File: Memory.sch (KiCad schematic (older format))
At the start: 8 parts, among them U2 24FC128, U3 W25Q128FW

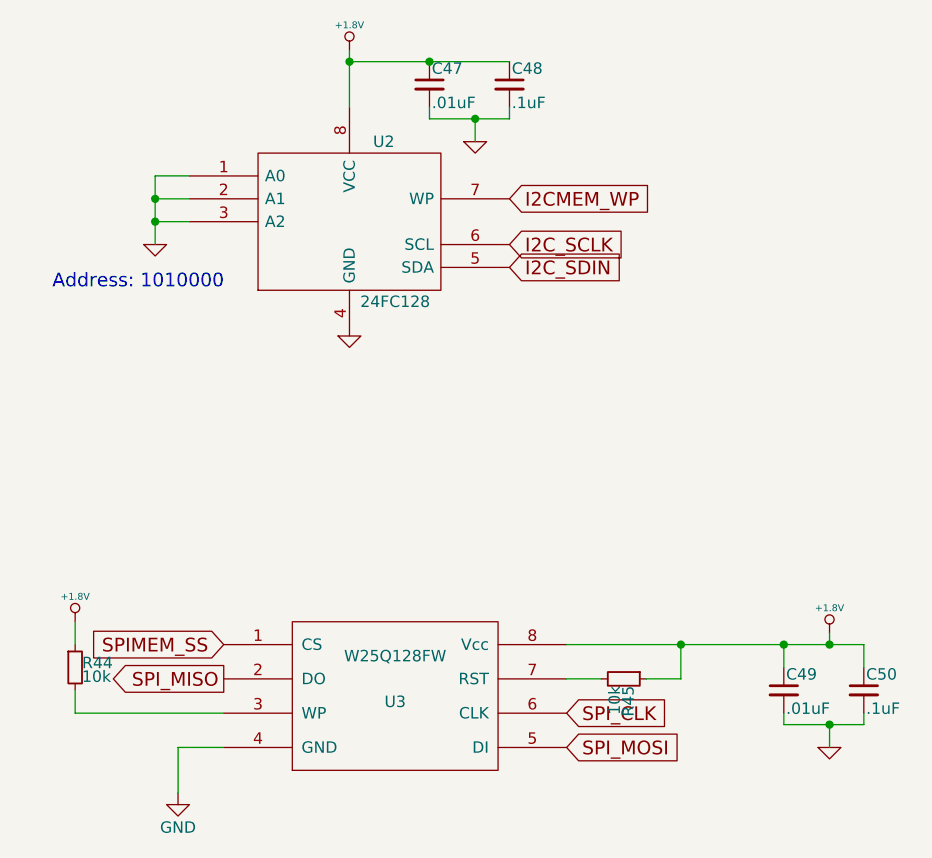
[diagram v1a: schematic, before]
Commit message: finished wiring GPIF with exception of PCLK
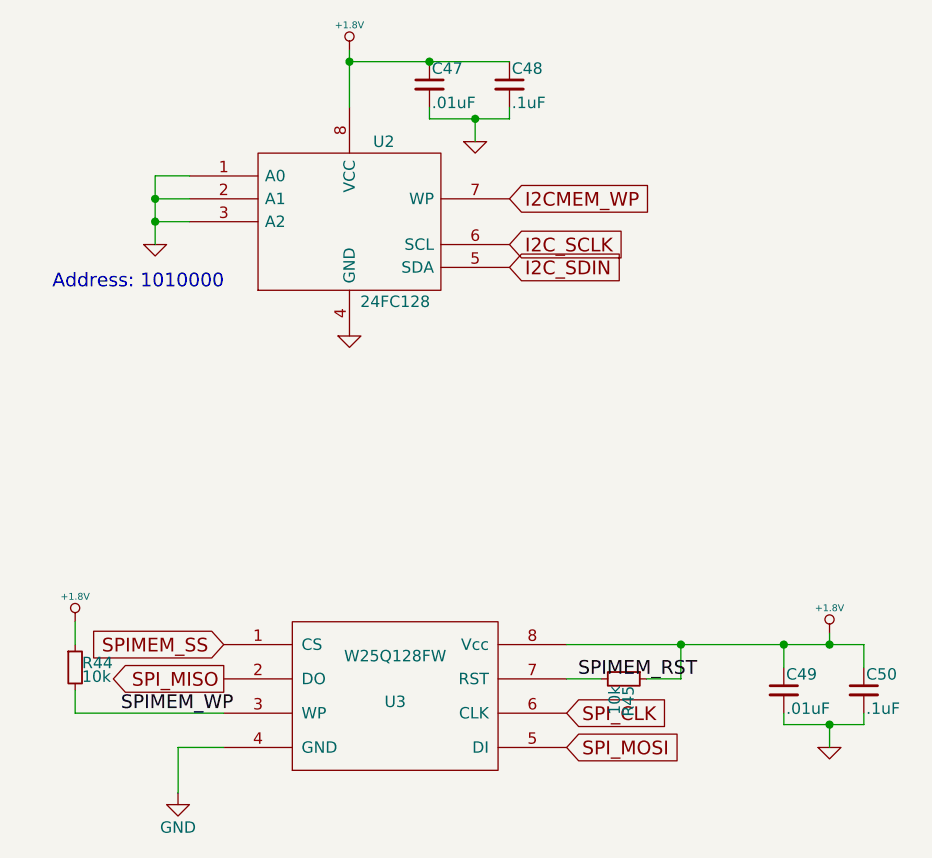
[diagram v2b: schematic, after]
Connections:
- net SPIMEM_WP: now reaches R44.2, U3.3 (WP)
- net SPIMEM_RST: now reaches R45.2, U3.7 (RST)
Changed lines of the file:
@@
 	6900 3850 6900 3700
 Connection ~ 6900 3700
+Text Label 6450 3850 0    60   ~ 0
+SPIMEM_RST
+Text Label 4450 4000 0    60   ~ 0
+SPIMEM_WP
 $EndSCHEMATC

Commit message: finished a quarter to a third of non-priority connections
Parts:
- R44, R45: footprint Resistors_SMD:R_1206 -> Resistors_SMD:R_0402
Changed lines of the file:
@@
 F 0 "R44" H 4280 3820 50  0000 L CNN
 F 1 "10k" H 4280 3760 50  0000 L CNN
-F 2 "Resistors_SMD:R_1206" H 4250 3800 50  0001 C CNN
+F 2 "Resistors_SMD:R_0402" H 4250 3800 50  0001 C CNN
 F 3 "" H 4250 3800 50  0000 C CNN
 	1    4250 3800
@@
 F 0 "R45" H 6680 3870 50  0000 L CNN
 F 1 "10k" H 6680 3810 50  0000 L CNN
-F 2 "Resistors_SMD:R_1206" H 6650 3850 50  0001 C CNN
+F 2 "Resistors_SMD:R_0402" H 6650 3850 50  0001 C CNN
 F 3 "" H 6650 3850 50  0000 C CNN
 	1    6650 3850

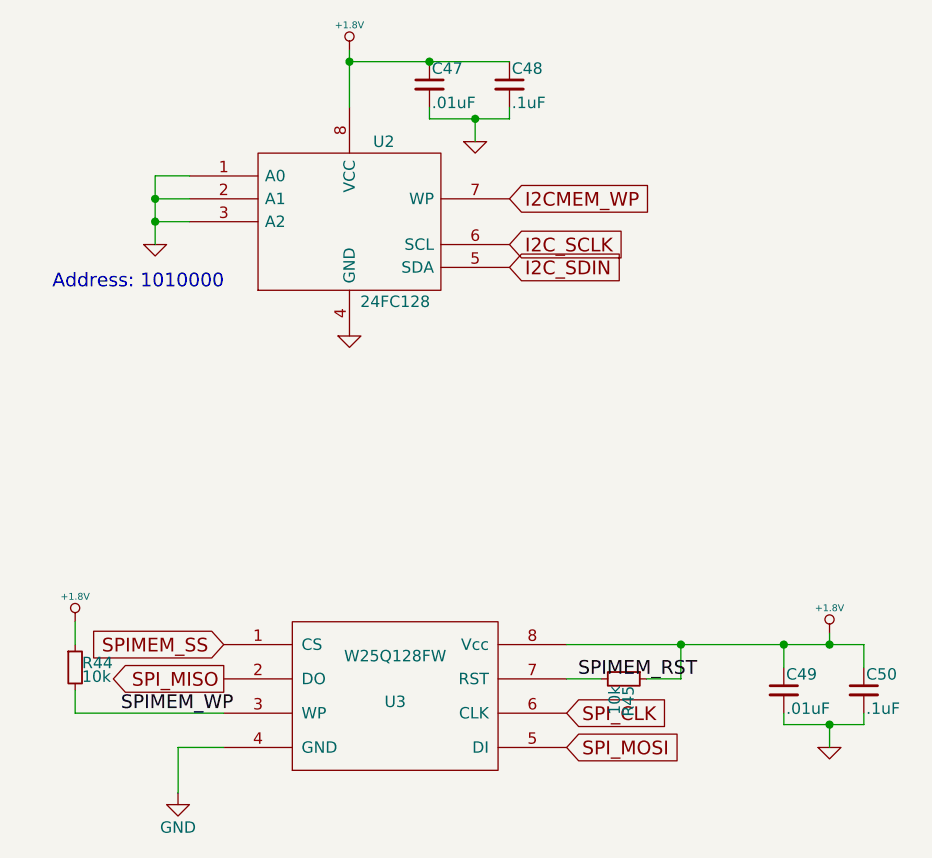
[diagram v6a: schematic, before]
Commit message: created output directory and outputs
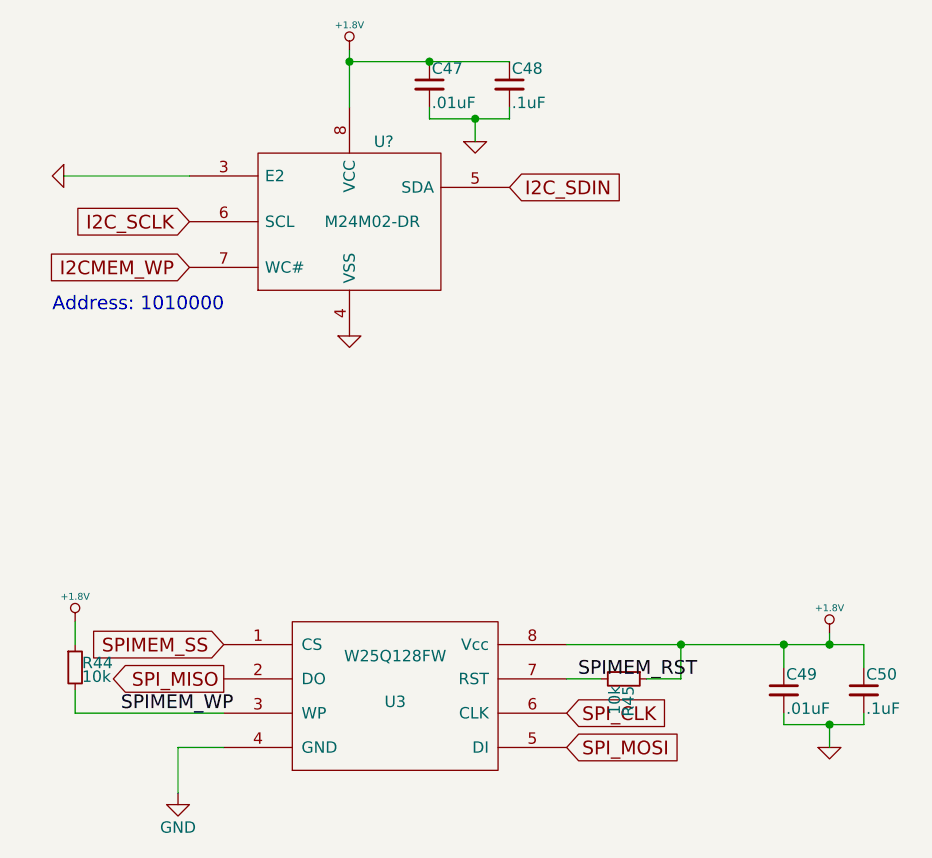
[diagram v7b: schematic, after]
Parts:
- removed U2: 24FC128, SMD_Packages:SOIC-8-N, symbol 24C512
- added U?: M24M02-DR, symbol M24M02-DR
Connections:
- net +1.8V: now also U?.8 (VCC)
- net GND: now also U?.3 (E2), U?.4 (VSS)
- net I2CMEM_WP: now also U?.7 (WC#)
- net I2C_SCLK: now also U?.6 (SCL)
- net I2C_SDIN: now also U?.5 (SDA)
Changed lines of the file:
@@
 LIBS:hdmi_conn
 LIBS:wayne_and_layne_kicad_symbols
+LIBS:m24m02-dr
 EELAYER 25 0
 EELAYER END
@@
 Comment4 ""
 $EndDescr
-$Comp
-L 24C512 U2
-U 1 1 5852F5FB
-P 5450 1850
-F 0 "U2" H 5600 2200 50  0000 C CNN
-F 1 "24FC128" H 5650 1500 50  0000 C CNN
-F 2 "SMD_Packages:SOIC-8-N" H 5450 1850 50  0001 C CNN
-F 3 "" H 5450 1850 50  0000 C CNN
-	1    5450 1850
-	1    0    0    -1
-$EndComp
-Text GLabel 6150 1950 2    60   Input ~ 0
+Text GLabel 4750 1850 0    60   Input ~ 0
 I2C_SCLK
-Text GLabel 6150 2050 2    60   Input ~ 0
+Text GLabel 6150 1700 2    60   Input ~ 0
 I2C_SDIN
 $Comp
-L +1.8V #PWR062
+L +1.8V #PWR063
 U 1 1 58594FA1
 P 5450 1100
-F 0 "#PWR062" H 5450 1240 20  0001 C CNN
+F 0 "#PWR063" H 5450 1240 20  0001 C CNN
 F 1 "+1.8V" H 5450 1210 30  0000 C CNN
 F 2 "" H 5450 1100 60  0001 C CNN
@@
 $EndComp
 $Comp
-L GND-RESCUE-DFTBoard #PWR063
+L GND-RESCUE-DFTBoard #PWR064
 U 1 1 58594FE3
-P 4600 1950
-F 0 "#PWR063" H 4600 1950 30  0001 C CNN
-F 1 "GND" H 4600 1880 30  0001 C CNN
-F 2 "" H 4600 1950 60  0001 C CNN
-F 3 "" H 4600 1950 60  0001 C CNN
-	1    4600 1950
-	1    0    0    -1
-$EndComp
-$Comp
-L GND-RESCUE-DFTBoard #PWR064
+P 4200 1650
+F 0 "#PWR064" H 4200 1650 30  0001 C CNN
+F 1 "GND" H 4200 1580 30  0001 C CNN
+F 2 "" H 4200 1650 60  0001 C CNN
+F 3 "" H 4200 1650 60  0001 C CNN
+	1    4200 1650
+	0    1    1    0
+$EndComp
+$Comp
+L GND-RESCUE-DFTBoard #PWR065
 U 1 1 58594FFB
 P 5450 2350
-F 0 "#PWR064" H 5450 2350 30  0001 C CNN
+F 0 "#PWR065" H 5450 2350 30  0001 C CNN
 F 1 "GND" H 5450 2280 30  0001 C CNN
 F 2 "" H 5450 2350 60  0001 C CNN
@@
 $EndComp
 Wire Wire Line
-	4750 1850 4600 1850
-Wire Wire Line
-	4600 1650 4600 1950
-Wire Wire Line
-	4750 1750 4600 1750
-Connection ~ 4600 1850
-Wire Wire Line
-	4750 1650 4600 1650
-Connection ~ 4600 1750
-Text Notes 4150 2150 0    60   ~ 0
+	4200 1650 4750 1650
+Text Notes 4150 2250 0    60   ~ 0
 Address: 1010000
-Text GLabel 6150 1750 2    60   Input ~ 0
+Text GLabel 4750 2050 0    60   Input ~ 0
 I2CMEM_WP
 Text GLabel 6400 4150 2    60   Input ~ 0
@@
 SPIMEM_SS
 $Comp
-L GND #PWR065
+L GND #PWR066
 U 1 1 58666BA4
 P 4700 4350
-F 0 "#PWR065" H 4700 4100 50  0001 C CNN
+F 0 "#PWR066" H 4700 4100 50  0001 C CNN
 F 1 "GND" H 4700 4200 50  0000 C CNN
 F 2 "" H 4700 4350 50  0000 C CNN
@@
 SPI_CLK
 $Comp
-L +1.8V #PWR066
+L +1.8V #PWR067
 U 1 1 5868C7CB
 P 7550 3650
-F 0 "#PWR066" H 7550 3790 20  0001 C CNN
+F 0 "#PWR067" H 7550 3790 20  0001 C CNN
 F 1 "+1.8V" H 7550 3760 30  0000 C CNN
 F 2 "" H 7550 3650 60  0001 C CNN
@@
 Connection ~ 5800 1150
 $Comp
-L GND-RESCUE-DFTBoard #PWR067
+L GND-RESCUE-DFTBoard #PWR068
 U 1 1 586C114A
 P 6000 1500
-F 0 "#PWR067" H 6000 1500 30  0001 C CNN
+F 0 "#PWR068" H 6000 1500 30  0001 C CNN
 F 1 "GND" H 6000 1430 30  0001 C CNN
 F 2 "" H 6000 1500 60  0001 C CNN
@@
 $EndComp
 $Comp
-L GND-RESCUE-DFTBoard #PWR068
+L GND-RESCUE-DFTBoard #PWR069
 U 1 1 586C1999
 P 7550 4150
-F 0 "#PWR068" H 7550 4150 30  0001 C CNN
+F 0 "#PWR069" H 7550 4150 30  0001 C CNN
 F 1 "GND" H 7550 4080 30  0001 C CNN
 F 2 "" H 7550 4150 60  0001 C CNN
@@
 	4900 4000 4250 4000
 $Comp
-L +1.8V #PWR069
+L +1.8V #PWR070
 U 1 1 5881768D
 P 4250 3600
-F 0 "#PWR069" H 4250 3740 20  0001 C CNN
+F 0 "#PWR070" H 4250 3740 20  0001 C CNN
 F 1 "+1.8V" H 4250 3710 30  0000 C CNN
 F 2 "" H 4250 3600 60  0001 C CNN
@@
 Text Label 4450 4000 0    60   ~ 0
 SPIMEM_WP
+$Comp
+L M24M02-DR U?
+U 1 1 5890D70E
+P 5450 1850
+F 0 "U?" H 5600 2200 50  0000 C CNN
+F 1 "M24M02-DR" H 5550 1850 50  0000 C CNN
+F 2 "" H 5450 1850 50  0000 C CNN
+F 3 "" H 5450 1850 50  0000 C CNN
+	1    5450 1850
+	1    0    0    -1
+$EndComp
 $EndSCHEMATC

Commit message: small changes, if any
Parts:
- U2: renamed from U?; footprint (none) -> Housings_SOIC:SOIC-8_3.9x4.9mm_Pitch1.27mm
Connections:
- net GND: no longer U2.3 (E2)
- no-connect marks 0 -> 1
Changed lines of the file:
@@
 $Comp
 L GND-RESCUE-DFTBoard #PWR064
-U 1 1 58594FE3
-P 4200 1650
-F 0 "#PWR064" H 4200 1650 30  0001 C CNN
-F 1 "GND" H 4200 1580 30  0001 C CNN
-F 2 "" H 4200 1650 60  0001 C CNN
-F 3 "" H 4200 1650 60  0001 C CNN
-	1    4200 1650
-	0    1    1    0
-$EndComp
-$Comp
-L GND-RESCUE-DFTBoard #PWR065
 U 1 1 58594FFB
 P 5450 2350
-F 0 "#PWR065" H 5450 2350 30  0001 C CNN
+F 0 "#PWR064" H 5450 2350 30  0001 C CNN
 F 1 "GND" H 5450 2280 30  0001 C CNN
 F 2 "" H 5450 2350 60  0001 C CNN
@@
 	1    0    0    -1
 $EndComp
-Wire Wire Line
-	4200 1650 4750 1650
 Text Notes 4150 2250 0    60   ~ 0
 Address: 1010000
@@
 SPIMEM_SS
 $Comp
-L GND #PWR066
+L GND #PWR065
 U 1 1 58666BA4
 P 4700 4350
-F 0 "#PWR066" H 4700 4100 50  0001 C CNN
+F 0 "#PWR065" H 4700 4100 50  0001 C CNN
 F 1 "GND" H 4700 4200 50  0000 C CNN
 F 2 "" H 4700 4350 50  0000 C CNN
@@
 SPI_CLK
 $Comp
-L +1.8V #PWR067
+L +1.8V #PWR066
 U 1 1 5868C7CB
 P 7550 3650
-F 0 "#PWR067" H 7550 3790 20  0001 C CNN
+F 0 "#PWR066" H 7550 3790 20  0001 C CNN
 F 1 "+1.8V" H 7550 3760 30  0000 C CNN
 F 2 "" H 7550 3650 60  0001 C CNN
@@
 Connection ~ 5800 1150
 $Comp
-L GND-RESCUE-DFTBoard #PWR068
+L GND-RESCUE-DFTBoard #PWR067
 U 1 1 586C114A
 P 6000 1500
-F 0 "#PWR068" H 6000 1500 30  0001 C CNN
+F 0 "#PWR067" H 6000 1500 30  0001 C CNN
 F 1 "GND" H 6000 1430 30  0001 C CNN
 F 2 "" H 6000 1500 60  0001 C CNN
@@
 $EndComp
 $Comp
-L GND-RESCUE-DFTBoard #PWR069
+L GND-RESCUE-DFTBoard #PWR068
 U 1 1 586C1999
 P 7550 4150
-F 0 "#PWR069" H 7550 4150 30  0001 C CNN
+F 0 "#PWR068" H 7550 4150 30  0001 C CNN
 F 1 "GND" H 7550 4080 30  0001 C CNN
 F 2 "" H 7550 4150 60  0001 C CNN
@@
 	4900 4000 4250 4000
 $Comp
-L +1.8V #PWR070
+L +1.8V #PWR069
 U 1 1 5881768D
 P 4250 3600
-F 0 "#PWR070" H 4250 3740 20  0001 C CNN
+F 0 "#PWR069" H 4250 3740 20  0001 C CNN
 F 1 "+1.8V" H 4250 3710 30  0000 C CNN
 F 2 "" H 4250 3600 60  0001 C CNN
@@
 SPIMEM_WP
 $Comp
-L M24M02-DR U?
+L M24M02-DR U2
 U 1 1 5890D70E
 P 5450 1850
-F 0 "U?" H 5600 2200 50  0000 C CNN
+F 0 "U2" H 5600 2200 50  0000 C CNN
 F 1 "M24M02-DR" H 5550 1850 50  0000 C CNN
-F 2 "" H 5450 1850 50  0000 C CNN
+F 2 "Housings_SOIC:SOIC-8_3.9x4.9mm_Pitch1.27mm" H 5450 1850 50  0001 C CNN
 F 3 "" H 5450 1850 50  0000 C CNN
 	1    5450 1850
 	1    0    0    -1
 $EndComp
+NoConn ~ 4750 1650
 $EndSCHEMATC
